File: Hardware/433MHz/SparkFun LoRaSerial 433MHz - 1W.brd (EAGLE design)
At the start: 50.8 x 27.4 mm, 118 parts, among them J1 QWIIC_RIGHT_ANGLE, J3 USB C, J4 JTAG, Q1 20V/0.2A/8MHz/1.2Ω/1Vth, Q2 20V/0.2A/8MHz/1.2Ω/1Vth, Q3 600mA/40V, Q4 600mA/40V, Q5 600mA/40V, Q6 600mA/40V, Q8 20V/4.2A/52mΩ/1.4W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

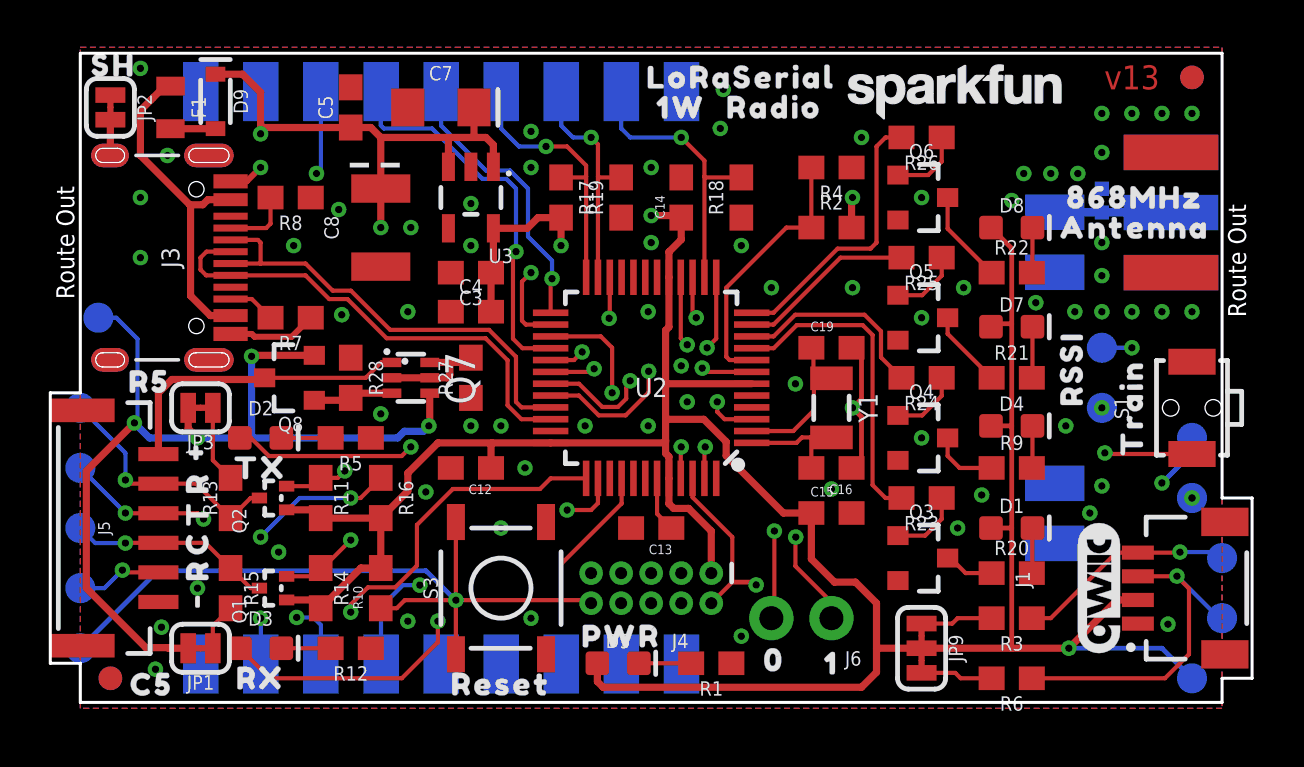
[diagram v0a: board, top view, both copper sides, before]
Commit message: Add 433MHz and 868MHz designs
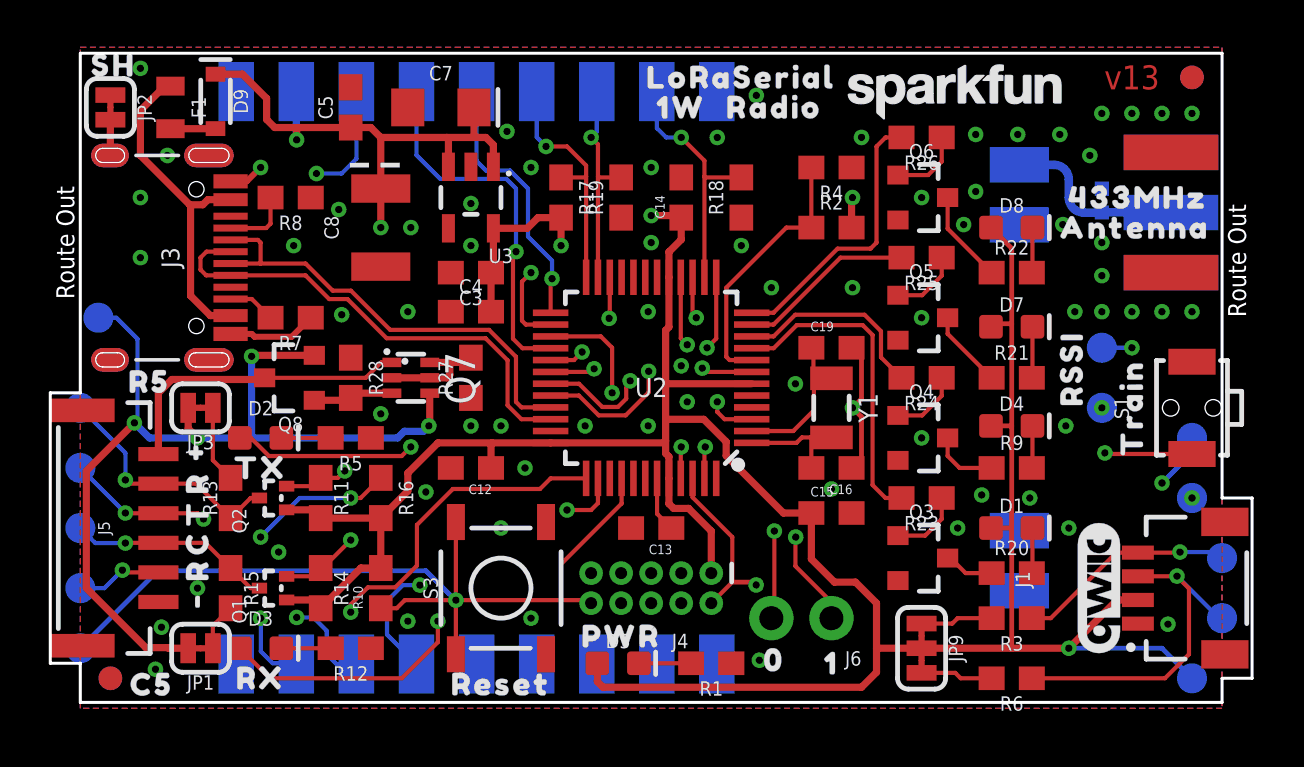
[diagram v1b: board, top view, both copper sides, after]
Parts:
- E2: value RP-SMA -> SMA; device SparkFun-RF:RP-SMA-EDGE -> SparkFun-RF:SMA-EDGE
- R2: value 3.3k -> 10k
- R4: value 10k -> 20k
- U$8: device output:868MHZ0 -> output:433MHZ0
- U4: device SparkFun-RF:E19-915M30S -> SparkFun-RF:E19-433M30S
- moved U$8 0.13 mm to (46.0, 21.6)
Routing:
- net LORA_ANT: track 4.92 -> 7.70 mm
- net D3/LORA_RXEN: track 12.2 -> 10.6 mm
- net D5/LORA_!CS!: track 11.6 -> 10.3 mm
- net D13/SPI_SCK: track 21.3 -> 22.5 mm
- net D6/LORA_!RST!: track 33.5 -> 34.7 mm
- net D7/LORA_D0: track 26.2 -> 27.3 mm
- net D2/LORA_TXEN: track 9.93 -> 9.07 mm
- net D12/SPI_POCI: track 16.4 -> 15.6 mm
- net D11/SPI_PICO: track 11.9 -> 11.3 mm

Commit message: Update schematics with flow control notes
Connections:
- net CTS-I_HV renamed !CTS!-I_HV
- net D30/CTS-I_LV renamed D30/!CTS!-I_LV
- net D38/RTS-O renamed D38/!RTS!-O
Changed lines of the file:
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@@
 <layers>
 <layer number="1" name="Top" color="4" fill="1" visible="yes" active="yes"/>
-<layer number="2" name="Digital" color="63" fill="3" visible="yes" active="yes"/>
-<layer number="15" name="GND" color="23" fill="6" visible="yes" active="yes"/>
+<layer number="2" name="Digital" color="63" fill="3" visible="no" active="yes"/>
+<layer number="15" name="GND" color="23" fill="6" visible="no" active="yes"/>
 <layer number="16" name="Bottom" color="1" fill="1" visible="yes" active="yes"/>
 <layer number="17" name="Pads" color="2" fill="1" visible="yes" active="yes"/>
@@
 <layer number="23" name="tOrigins" color="15" fill="1" visible="yes" active="yes"/>
 <layer number="24" name="bOrigins" color="15" fill="1" visible="yes" active="yes"/>
-<layer number="25" name="tNames" color="7" fill="1" visible="yes" active="yes"/>
-<layer number="26" name="bNames" color="7" fill="1" visible="yes" active="yes"/>
-<layer number="27" name="tValues" color="7" fill="1" visible="yes" active="yes"/>
-<layer number="28" name="bValues" color="7" fill="1" visible="yes" active="yes"/>
-<layer number="29" name="tStop" color="7" fill="3" visible="yes" active="yes"/>
-<layer number="30" name="bStop" color="7" fill="6" visible="yes" active="yes"/>
-<layer number="31" name="tCream" color="7" fill="4" visible="yes" active="yes"/>
-<layer number="32" name="bCream" color="7" fill="5" visible="yes" active="yes"/>
-<layer number="33" name="tFinish" color="6" fill="3" visible="yes" active="yes"/>
-<layer number="34" name="bFinish" color="6" fill="6" visible="yes" active="yes"/>
-<layer number="35" name="tGlue" color="7" fill="4" visible="yes" active="yes"/>
-<layer number="36" name="bGlue" color="7" fill="5" visible="yes" active="yes"/>
-<layer number="37" name="tTest" color="7" fill="1" visible="yes" active="yes"/>
-<layer number="38" name="bTest" color="7" fill="1" visible="yes" active="yes"/>
-<layer number="39" name="tKeepout" color="4" fill="11" visible="yes" active="yes"/>
-<layer number="40" name="bKeepout" color="1" fill="11" visible="yes" active="yes"/>
-<layer number="41" name="tRestrict" color="4" fill="10" visible="yes" active="yes"/>
-<layer number="42" name="bRestrict" color="1" fill="10" visible="yes" active="yes"/>
-<layer number="43" name="vRestrict" color="2" fill="10" visible="yes" active="yes"/>
-<layer number="44" name="Drills" color="7" fill="1" visible="yes" active="yes"/>
+<layer number="25" name="tNames" color="7" fill="1" visible="no" active="yes"/>
+<layer number="26" name="bNames" color="7" fill="1" visible="no" active="yes"/>
+<layer number="27" name="tValues" color="7" fill="1" visible="no" active="yes"/>
+<layer number="28" name="bValues" color="7" fill="1" visible="no" active="yes"/>
+<layer number="29" name="tStop" color="7" fill="3" visible="no" active="yes"/>
+<layer number="30" name="bStop" color="7" fill="6" visible="no" active="yes"/>
+<layer number="31" name="tCream" color="7" fill="4" visible="no" active="yes"/>
+<layer number="32" name="bCream" color="7" fill="5" visible="no" active="yes"/>
+<layer number="33" name="tFinish" color="6" fill="3" visible="no" active="yes"/>
+<layer number="34" name="bFinish" color="6" fill="6" visible="no" active="yes"/>
+<layer number="35" name="tGlue" color="7" fill="4" visible="no" active="yes"/>
+<layer number="36" name="bGlue" color="7" fill="5" visible="no" active="yes"/>
+<layer number="37" name="tTest" color="7" fill="1" visible="no" active="yes"/>
+<layer number="38" name="bTest" color="7" fill="1" visible="no" active="yes"/>
+<layer number="39" name="tKeepout" color="4" fill="11" visible="no" active="yes"/>
+<layer number="40" name="bKeepout" color="1" fill="11" visible="no" active="yes"/>
+<layer number="41" name="tRestrict" color="4" fill="10" visible="no" active="yes"/>
+<layer number="42" name="bRestrict" color="1" fill="10" visible="no" active="yes"/>
+<layer number="43" name="vRestrict" color="2" fill="10" visible="no" active="yes"/>
+<layer number="44" name="Drills" color="7" fill="1" visible="no" active="yes"/>
 <layer number="45" name="Holes" color="7" fill="1" visible="yes" active="yes"/>
-<layer number="46" name="Milling" color="3" fill="1" visible="yes" active="yes"/>
-<layer number="47" name="Measures" color="7" fill="1" visible="yes" active="yes"/>
-<layer number="48" name="Document" color="7" fill="1" visible="yes" active="yes"/>
-<layer number="49" name="Reference" color="7" fill="1" visible="yes" active="yes"/>
-<layer number="50" name="dxf" color="7" fill="1" visible="yes" active="yes"/>
+<layer number="46" name="Milling" color="3" fill="1" visible="no" active="yes"/>
+<layer number="47" name="Measures" color="7" fill="1" visible="no" active="yes"/>
+<layer number="48" name="Document" color="7" fill="1" visible="no" active="yes"/>
+<layer number="49" name="Reference" color="7" fill="1" visible="no" active="yes"/>
+<layer number="50" name="dxf" color="7" fill="1" visible="no" active="yes"/>
 <layer number="51" name="tDocu" color="6" fill="1" visible="yes" active="yes"/>
-<layer number="52" name="bDocu" color="7" fill="1" visible="yes" active="yes"/>
+<layer number="52" name="bDocu" color="7" fill="1" visible="no" active="yes"/>
 <layer number="91" name="Nets" color="2" fill="1" visible="no" active="no"/>
 <layer number="92" name="Busses" color="1" fill="1" visible="no" active="no"/>
@@
 <wire x1="26.1239" y1="11.6459" x2="18.161" y2="3.683" width="0.1778" layer="2"/>
 </signal>
-<signal name="D30/CTS-I_LV">
+<signal name="D30/!CTS!-I_LV">
 <contactref element="U2" pad="37"/>
 <contactref element="R14" pad="1"/>
@@
 <contactref element="U2" pad="21"/>
 </signal>
-<signal name="D38/RTS-O">
+<signal name="D38/!RTS!-O">
 <contactref element="U2" pad="22"/>
 <contactref element="J5" pad="5"/>
@@
 <wire x1="3.175" y1="10.795" x2="3.175" y2="9.652" width="0.1778" layer="16"/>
 </signal>
-<signal name="CTS-I_HV">
+<signal name="!CTS!-I_HV">
 <contactref element="J5" pad="4"/>
 <contactref element="Q1" pad="3"/>
